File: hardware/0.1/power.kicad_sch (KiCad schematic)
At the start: 61 parts

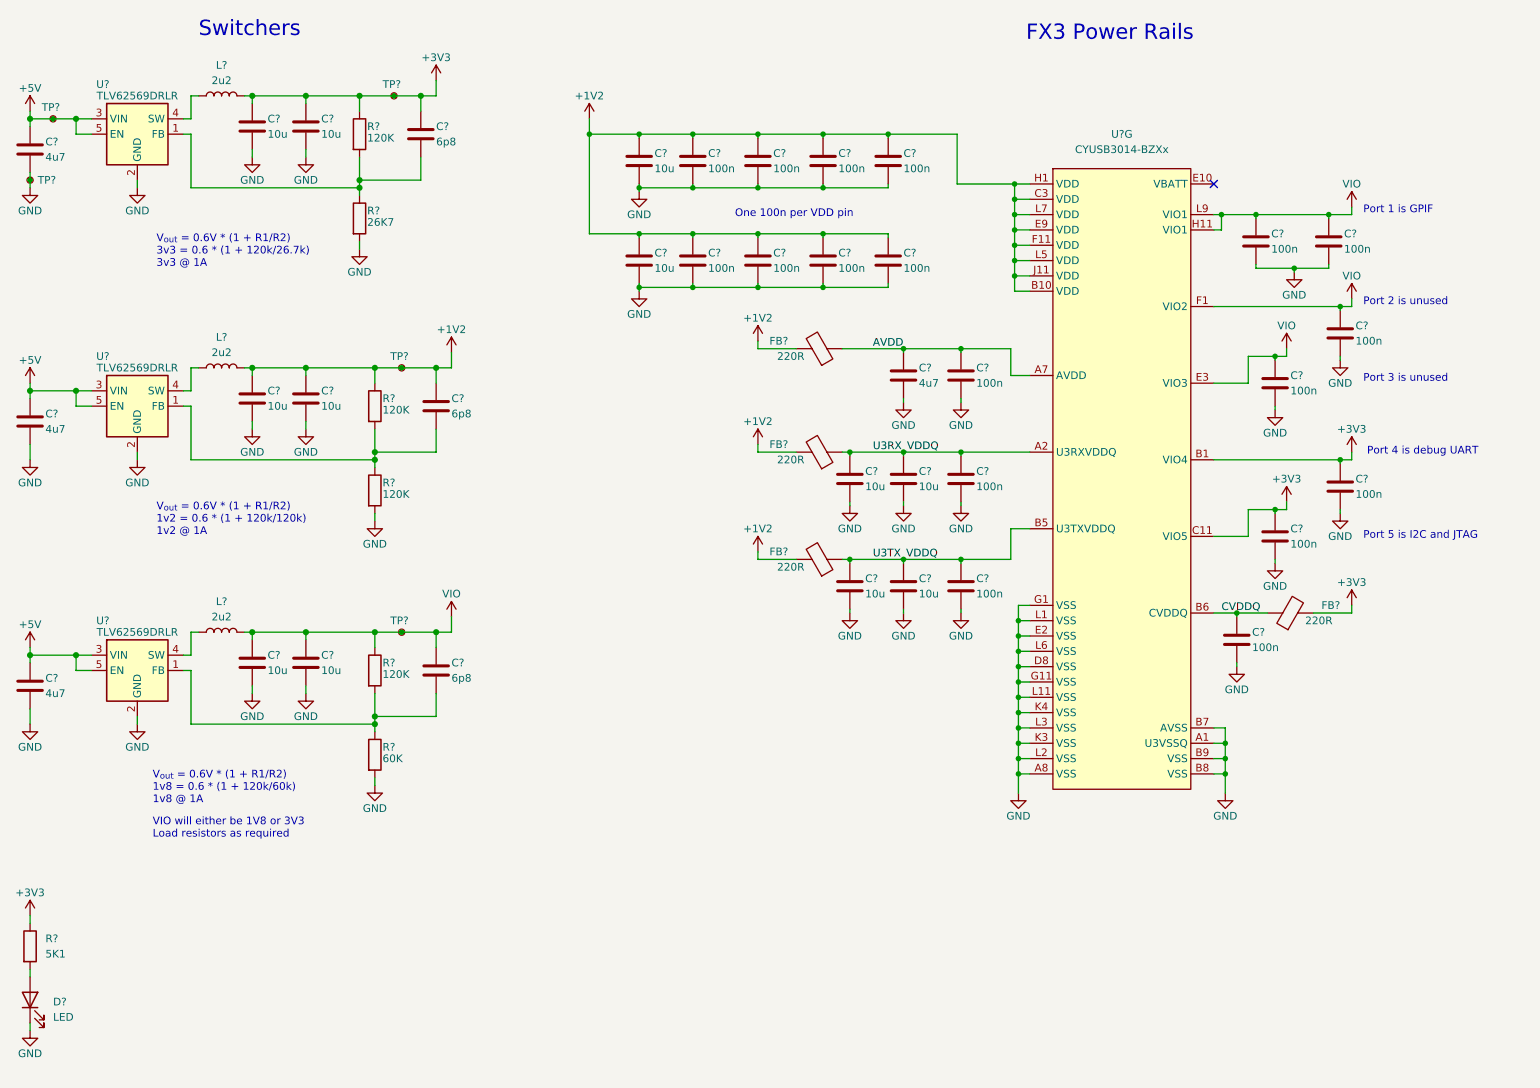
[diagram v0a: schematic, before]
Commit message: first pass schematic done
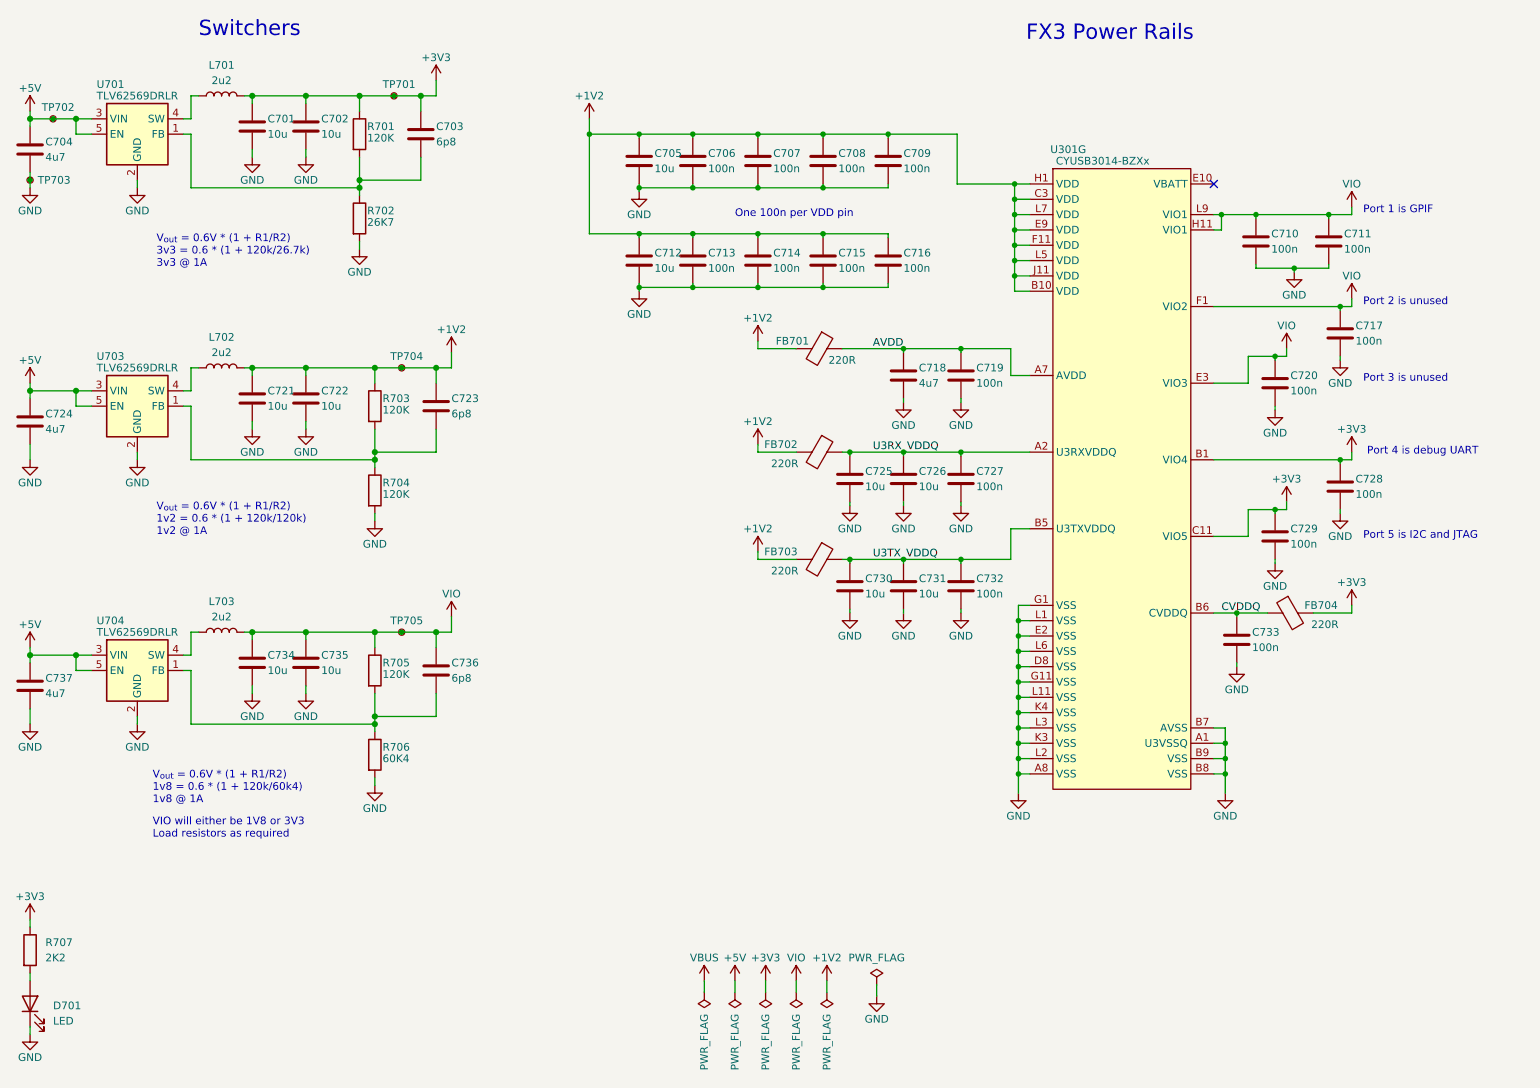
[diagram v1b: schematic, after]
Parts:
- removed FB? (x4): 220R, symbol Device:FerriteBead
- added FB701, FB702, FB703, FB704: 220R, Resistor_SMD:R_0402_1005Metric, symbol josh-passive:Ferrite_Bead_PWR
- C701, C702, C705, C712, C721, C722, C725, C726, C730, C731, C734, C735: renamed from C?; LCSC C109453 -> C96446; MPN CC0603MRX5R6BB106 -> CL10A106MA8NRNC; Manufacturer Yageo -> Samsung Electro-Mechanics; Manufacturer2 Samsung Electro-Mechanics -> (none)
- C703, C723, C736: renamed from C?; LCSC C327291 -> C1525; MPN CC0402KRX7R9BB682 -> CL05B104KO5NNNC; MPN2 CL05B682KA5NNNC -> (none); Manufacturer Yageo -> Samsung Electro-Mechanics
- C704, C724, C737: renamed from C?; LCSC C326586 -> C23733; MPN CC0402KRX5R6BB475 -> CL05A475MP5NRNC; Manufacturer Yageo -> Samsung Electro-Mechanics; Manufacturer2 Samsung Electro-Mechanics -> (none)
- C706, C707, C708, C709, C710, C711, C713, C714, C715, C716, C717, C719, C720, C727, C728, C729, C732, C733: renamed from C?; footprint (none) -> Capacitor_SMD:C_0402_1005Metric; LCSC (none) -> C307331; MPN (none) -> CL05B104KB54PNC; Manufacturer (none) -> Samsung Electro-Mechanics
- C718: renamed from C?; footprint Capacitor_SMD:C_0603_1608Metric -> Capacitor_SMD:C_0402_1005Metric; LCSC C109453 -> C23733; MPN CC0603MRX5R6BB106 -> CL05A475MP5NRNC; Manufacturer Yageo -> Samsung Electro-Mechanics; Manufacturer2 Samsung Electro-Mechanics -> (none)
- D701: renamed from D?; footprint (none) -> LED_SMD:LED_0603_1608Metric; MPN (none) -> OSK40603C1E; Manufacturer (none) -> OptoSupply
- L701, L702, L703: renamed from L?; Manufacturer (none) -> Murata Electronics; Manufacturer2 Sunltech Tech -> (none)
- R701, R703, R704, R705: renamed from R?; LCSC (none) -> C93945; MPN2 0402WGF1203TCE -> (none); Manufacturer2 UNI-ROYAL(Uniroyal Elec) -> (none)
- R702: renamed from R?; LCSC (none) -> C138023; MPN2 ERJ-2RKF2672X -> (none); Manufacturer2 Panasonic -> (none)
- R706: renamed from R?; value 60K -> 60K4; LCSC (none) -> C327333; MPN RC0402FR-07120KL -> RC0402FR-0760K4L; MPN2 0402WGF1203TCE -> (none); Manufacturer2 UNI-ROYAL(Uniroyal Elec) -> (none)
- R707: renamed from R?; value 5K1 -> 2K2; footprint (none) -> Resistor_SMD:R_0402_1005Metric; LCSC (none) -> C114762; MPN (none) -> RC0402FR-072K2L; Manufacturer (none) -> Yageo
- TP701, TP702, TP704, TP705: renamed from TP?; footprint (none) -> josh-test-point:TestPoint_SMDPad_D1.0mm_NO_SILK; now left out of the parts list
- TP703: renamed from TP?; footprint (none) -> josh-test-point:S1751-46_smdTestPoint; Digikey (none) -> 952-3024-ND; MPN (none) -> S1751-46; Manufacturer (none) -> Harwin
- U301: renamed from U?; footprint (none) -> josh-bga:BGA-121_10x10mm_Layout11x11_P0.8mm; Digikey (none) -> 448-CYUSB3014-BZXC-ND; LCSC (none) -> C462526; MPN (none) -> CYUSB3014-BZXC; Manufacturer (none) -> Cypress / Infineon
- U701, U703, U704: renamed from U?; Digikey (none) -> 296-48981-1-ND
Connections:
- net +1V2: now also FB701.2, FB702.2, FB703.2
- net +3V3: now also FB704.2
- net AVDD: now also FB701.1
- net CVDDQ: now also FB704.1
- net U3RX_VDDQ: now also FB702.1
- net U3TX_VDDQ: now also FB703.1
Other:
- note added: "V_{out} = 0.6V * (1 + R1/R2) 1v8 = 0.6 * (1 + 120k/60k4) 1v8 @ 1A"
- note removed: "V_{out} = 0.6V * (1 + R1/R2) 1v8 = 0.6 * (1 + 120k/60k) 1v8 @ 1A"
- company: (none) -> Josh Johnson
- title: (none) -> Voyager Logic
- moved on the sheet: D701, R707

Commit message: finalise BOM
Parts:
- removed D701: LED, LED_SMD:LED_0603_1608Metric, symbol Device:LED
- removed R707: 2K2, Resistor_SMD:R_0402_1005Metric, symbol Device:R
- TP701, TP702, TP704, TP705: footprint josh-test-point:TestPoint_SMDPad_D1.0mm_NO_SILK -> josh-test-point:TestPoint_SMDPad_D0.5mm_NO_SILK
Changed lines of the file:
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@@
     (stroke (width 0) (type default) (color 0 0 0 0))
   )
-  (wire (pts (xy 27.305 169.545) (xy 27.305 170.815))
-    (stroke (width 0) (type default) (color 0 0 0 0))
-  )
   (wire (pts (xy 181.61 74.93) (xy 189.865 74.93))
     (stroke (width 0) (type default) (color 0 0 0 0))
@@
     (stroke (width 0) (type solid) (color 0 0 0 0))
   )
-  (wire (pts (xy 27.305 187.325) (xy 27.305 188.595))
-    (stroke (width 0) (type default) (color 0 0 0 0))
-  )
   (wire (pts (xy 128.27 48.26) (xy 137.16 48.26))
     (stroke (width 0) (type default) (color 0 0 0 0))
@@
     (stroke (width 0) (type solid) (color 0 0 0 0))
   )
-  (wire (pts (xy 27.305 178.435) (xy 27.305 179.705))
-    (stroke (width 0) (type default) (color 0 0 0 0))
-  )
   (wire (pts (xy 64.135 78.105) (xy 64.135 79.375))
     (stroke (width 0) (type solid) (color 0 0 0 0))
@@
     (pin "1")
   )
-  (symbol (lib_id "Device:LED") (at 27.305 183.515 90) (unit 1)
-    (in_bom yes) (on_board yes) (fields_autoplaced)
-    (property "Reference" "D701" (id 0) (at 31.115 183.8324 90)
-      (effects (font (size 1.27 1.27)) (justify right))
-    )
-    (property "Value" "LED" (id 1) (at 31.115 186.3724 90)
-      (effects (font (size 1.27 1.27)) (justify right))
-    )
-    (property "Footprint" "LED_SMD:LED_0603_1608Metric" (id 2) (at 27.305 183.515 0)
-      (effects (font (size 1.27 1.27)) hide)
-    )
-    (property "Datasheet" "~" (id 3) (at 27.305 183.515 0)
-      (effects (font (size 1.27 1.27)) hide)
-    )
-    (property "MPN" "OSK40603C1E" (id 4) (at 27.305 183.515 0)
-      (effects (font (size 1.27 1.27)) hide)
-    )
-    (property "Manufacturer" "OptoSupply" (id 5) (at 27.305 183.515 0)
-      (effects (font (size 1.27 1.27)) hide)
-    )
-    (pin "1")
-    (pin "2")
-  )
   (symbol (lib_id "Connector:TestPoint_Small") (at 31.115 36.83 0) (unit 1)
     (in_bom no) (on_board yes)
@@
       (effects (font (size 1.27 1.27)) (justify left) hide)
     )
-    (property "Footprint" "josh-test-point:TestPoint_SMDPad_D1.0mm_NO_SILK" (id 2) (at 36.195 36.83 0)
+    (property "Footprint" "josh-test-point:TestPoint_SMDPad_D0.5mm_NO_SILK" (id 2) (at 36.195 36.83 0)
       (effects (font (size 1.27 1.27)) hide)
     )
@@
     (pin "2")
   )
-  (symbol (lib_id "power:+3V3") (at 27.305 169.545 0) (unit 1)
-    (in_bom yes) (on_board yes)
-    (property "Reference" "#PWR0750" (id 0) (at 27.305 173.355 0)
-      (effects (font (size 1.27 1.27)) hide)
-    )
-    (property "Value" "+3V3" (id 1) (at 27.305 165.735 0))
-    (property "Footprint" "" (id 2) (at 27.305 169.545 0)
-      (effects (font (size 1.27 1.27)) hide)
-    )
-    (property "Datasheet" "" (id 3) (at 27.305 169.545 0)
-      (effects (font (size 1.27 1.27)) hide)
-    )
-    (pin "1")
-  )
   (symbol (lib_id "power:GND") (at 172.085 83.82 0) (unit 1)
     (in_bom yes) (on_board yes)
@@
     (pin "2")
   )
-  (symbol (lib_id "Device:R") (at 27.305 174.625 0) (unit 1)
-    (in_bom yes) (on_board yes) (fields_autoplaced)
-    (property "Reference" "R707" (id 0) (at 29.845 173.3549 0)
-      (effects (font (size 1.27 1.27)) (justify left))
-    )
-    (property "Value" "2K2" (id 1) (at 29.845 175.8949 0)
-      (effects (font (size 1.27 1.27)) (justify left))
-    )
-    (property "Footprint" "Resistor_SMD:R_0402_1005Metric" (id 2) (at 25.527 174.625 90)
-      (effects (font (size 1.27 1.27)) hide)
-    )
-    (property "Datasheet" "~" (id 3) (at 27.305 174.625 0)
-      (effects (font (size 1.27 1.27)) hide)
-    )
-    (property "LCSC" "C114762" (id 4) (at 27.305 174.625 0)
-      (effects (font (size 1.27 1.27)) hide)
-    )
-    (property "MPN" "RC0402FR-072K2L" (id 5) (at 27.305 174.625 0)
-      (effects (font (size 1.27 1.27)) hide)
-    )
-    (property "Manufacturer" "Yageo" (id 6) (at 27.305 174.625 0)
-      (effects (font (size 1.27 1.27)) hide)
-    )
-    (pin "1")
-    (pin "2")
-  )
   (symbol (lib_id "power:+3V3") (at 235.585 100.33 0) (unit 1)
     (in_bom yes) (on_board yes)
@@
       (effects (font (size 1.27 1.27)) (justify left) hide)
     )
-    (property "Footprint" "josh-test-point:TestPoint_SMDPad_D1.0mm_NO_SILK" (id 2) (at 93.98 121.92 0)
+    (property "Footprint" "josh-test-point:TestPoint_SMDPad_D0.5mm_NO_SILK" (id 2) (at 93.98 121.92 0)
       (effects (font (size 1.27 1.27)) hide)
     )
@@
       (effects (font (size 1.27 1.27)) (justify left) hide)
     )
-    (property "Footprint" "josh-test-point:TestPoint_SMDPad_D1.0mm_NO_SILK" (id 2) (at 92.71 33.02 0)
+    (property "Footprint" "josh-test-point:TestPoint_SMDPad_D0.5mm_NO_SILK" (id 2) (at 92.71 33.02 0)
       (effects (font (size 1.27 1.27)) hide)
     )
@@
       (effects (font (size 1.27 1.27)) (justify left) hide)
     )
-    (property "Footprint" "josh-test-point:TestPoint_SMDPad_D1.0mm_NO_SILK" (id 2) (at 93.98 78.105 0)
+    (property "Footprint" "josh-test-point:TestPoint_SMDPad_D0.5mm_NO_SILK" (id 2) (at 93.98 78.105 0)
       (effects (font (size 1.27 1.27)) hide)
     )
@@
     (pin "2")
   )
-  (symbol (lib_id "power:GND") (at 27.305 188.595 0) (unit 1)
-    (in_bom yes) (on_board yes)
-    (property "Reference" "#PWR0751" (id 0) (at 27.305 194.945 0)
-      (effects (font (size 1.27 1.27)) hide)
-    )
-    (property "Value" "GND" (id 1) (at 27.305 192.405 0))
-    (property "Footprint" "" (id 2) (at 27.305 188.595 0)
-      (effects (font (size 1.27 1.27)) hide)
-    )
-    (property "Datasheet" "" (id 3) (at 27.305 188.595 0)
-      (effects (font (size 1.27 1.27)) hide)
-    )
-    (pin "1")
-  )
   (symbol (lib_id "power:PWR_FLAG") (at 144.145 181.61 180) (unit 1)

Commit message: all components fit inside outline
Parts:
- U701, U703, U704: footprint Package_TO_SOT_SMD:SOT-563 -> josh-soic-sot-etc:SOT-563
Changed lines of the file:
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@@
     (property "Reference" "U704" (id 0) (at 40.64 120.015 0))
     (property "Value" "TLV62569DRLR" (id 1) (at 45.085 121.92 0))
-    (property "Footprint" "Package_TO_SOT_SMD:SOT-563" (id 2) (at 46.355 134.62 0)
+    (property "Footprint" "josh-soic-sot-etc:SOT-563" (id 2) (at 46.355 134.62 0)
       (effects (font (size 1.27 1.27) italic) (justify left) hide)
     )
@@
     (property "Reference" "U701" (id 0) (at 40.64 31.115 0))
     (property "Value" "TLV62569DRLR" (id 1) (at 45.085 33.02 0))
-    (property "Footprint" "Package_TO_SOT_SMD:SOT-563" (id 2) (at 46.355 45.72 0)
+    (property "Footprint" "josh-soic-sot-etc:SOT-563" (id 2) (at 46.355 45.72 0)
       (effects (font (size 1.27 1.27) italic) (justify left) hide)
     )
@@
     (property "Reference" "U703" (id 0) (at 40.64 76.2 0))
     (property "Value" "TLV62569DRLR" (id 1) (at 45.085 78.105 0))
-    (property "Footprint" "Package_TO_SOT_SMD:SOT-563" (id 2) (at 46.355 90.805 0)
+    (property "Footprint" "josh-soic-sot-etc:SOT-563" (id 2) (at 46.355 90.805 0)
       (effects (font (size 1.27 1.27) italic) (justify left) hide)
     )
